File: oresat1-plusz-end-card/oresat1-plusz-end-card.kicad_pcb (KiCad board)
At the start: 4 copper layers, 99.8 x 94.6 mm, 103 parts, among them J1 J-SAMTEC-TFM-120-01-L-D-RA, J2 M55-7101242R, J3 M55-7101242R, J4 M55-7101242R, J5 M55-7101242R, J6 U.FL-R-SMT-1, Q1 DMP2240UDM, Q11 DMP2240UDM-7, Q2 PMV45EN, Q3 PMV45EN, Q4 PMV45EN, Q6 PMV45EN, Q9 DMP2240UDM-7, U11 MIC842LYC5, U12 MIC842LYC5, U2 MAX7310, U201 TS5A21366, U202 TS5A21366, U203 TS5A21366, U204 TS5A21366

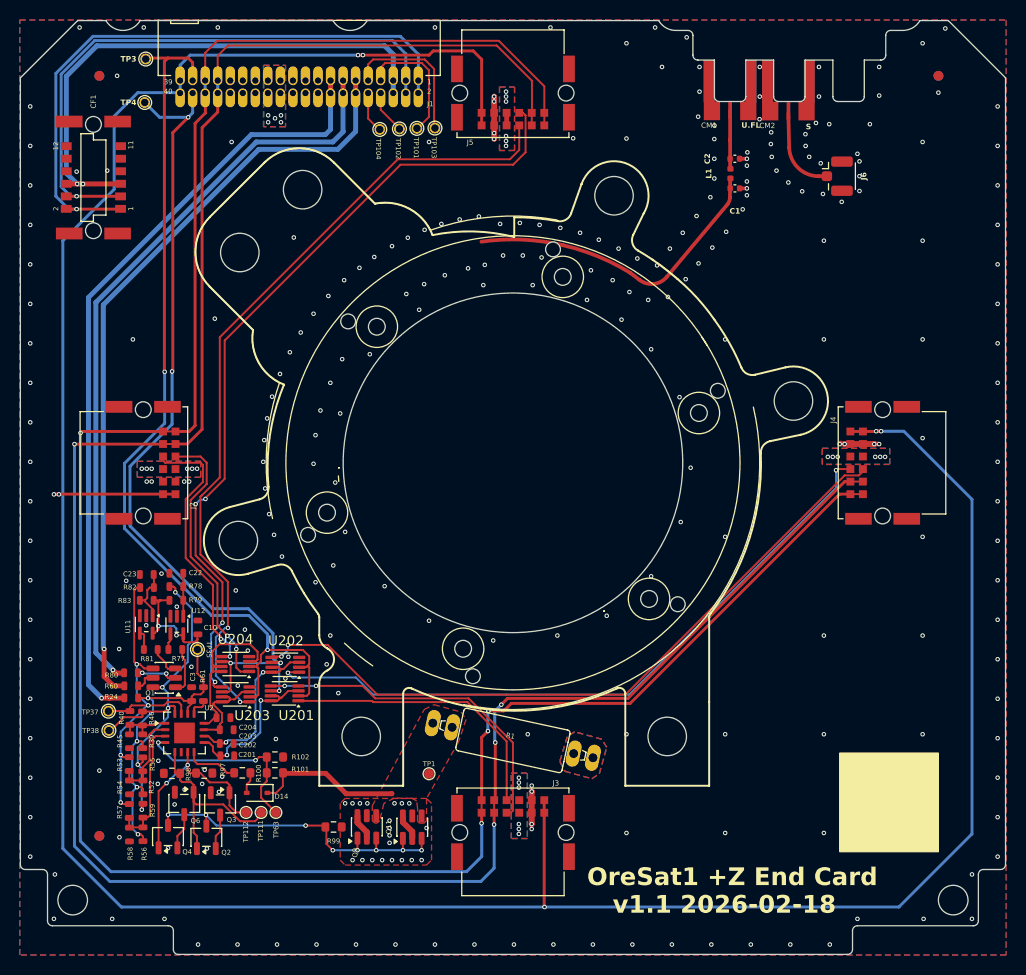
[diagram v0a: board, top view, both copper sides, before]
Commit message: Another round on the +Z End Card; ready for fab.
Brushed up RF paths and solder mask, cleaned up UART switches with closer bypass caps, cleaned up a lot of the zones, and lots of little polishing.
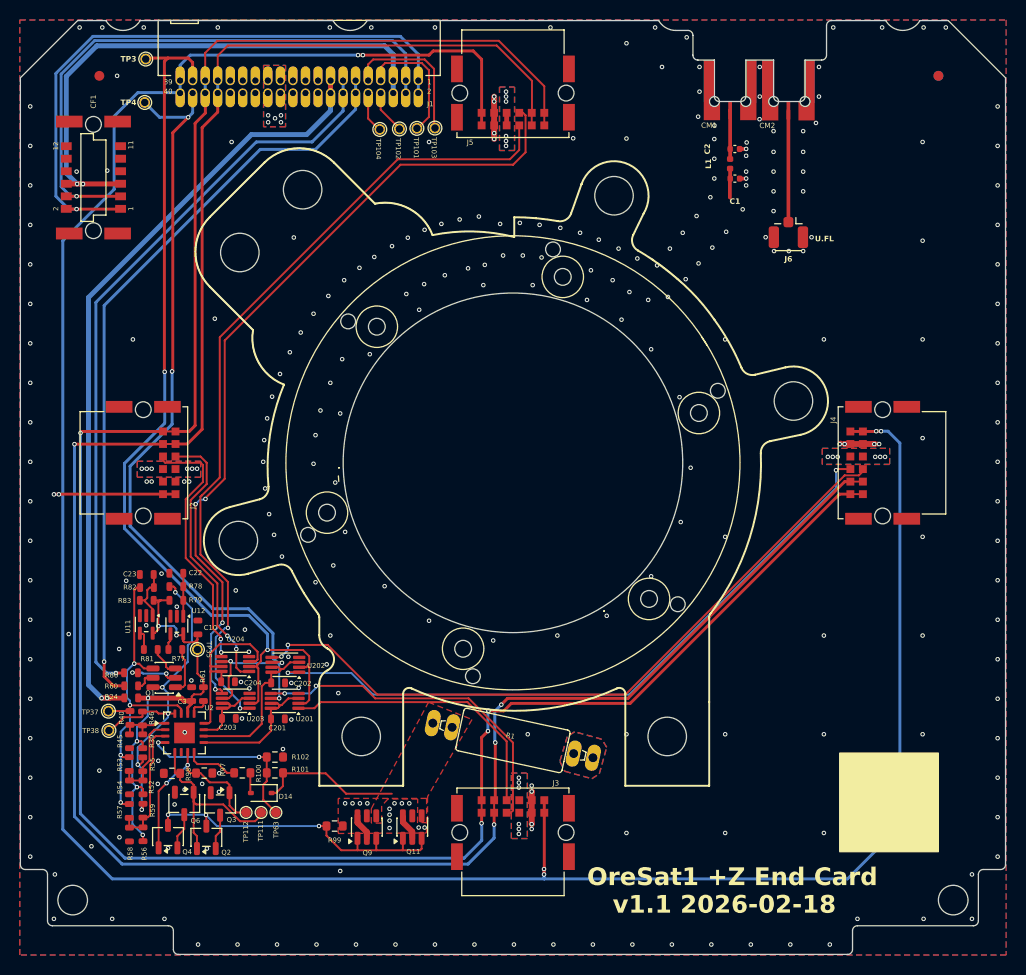
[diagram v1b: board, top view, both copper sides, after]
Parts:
- removed FID4, FID5, FID6: Fiducial, Fiducial:Fiducial_1mm_Mask2mm
- removed TP1: Test-Point, oresat-misc:TestPoint_Pad_D1.0mm
- PCB1: footprint oresat-pcbs:ORESAT-CARD-V1.3-3RF -> oresat-pcbs:ORESAT-CARD-V1.3-2RF-LEFT
- Q1: value DMP2240UDM -> DMP2240UDM-7
- Q2, Q3, Q4, Q6: value PMV45EN -> DMN3028LQ-7
- R39, R40, R45, R46, R52, R53, R54, R55, R56, R57, R58, R59: value 1k -> 100
- moved C202 8.05 mm to (124.7, 124.8)
- moved J6 7.55 mm to (176.4, 79.2), turned to -90 degrees
- moved C201 6.35 mm to (124.7, 128.4)
- moved C204 3.67 mm to (119.6, 124.7)
- moved C203 1.16 mm to (119.7, 128.4)
- moved L1 0.99 mm to (170.5, 72.2)
- moved C1 0.99 mm to (171.0, 73.7)
- moved C2 0.99 mm to (171.0, 70.7)
- moved U201 0.76 mm to (125.4, 126.6)
- moved U203 0.65 mm to (120.4, 126.6)
- moved D14 0.42 mm to (123.0, 135.9)
- moved R99 0.14 mm to (130.4, 139.3)
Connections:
- net /HELICAL renamed RF_HELICAL_ANT
- net /PATCH renamed /RF_PATCH
- net Net-(C2-Pad2) renamed /RF_HELICAL
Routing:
- net /~{SD}: track 296.9 -> 279.3 mm, vias 7 -> 8
- net /RF_PATCH: track 0.00 -> 11.3 mm
- net /CAN1_H: track 238.5 -> 233.5 mm
- net /CAN1_L: track 236.9 -> 233.2 mm
- net /C3_UART_RX: track 88.4 -> 90.8 mm
- net /OPD/PX_UART_EN: track 16.6 -> 14.6 mm, vias 2 -> 0
- net /OPD/MX_UART_EN: track 9.92 -> 8.00 mm
- net /OPD_SDA: track 78.1 -> 76.6 mm
- net /C3_UART_TX: track 94.3 -> 95.6 mm
- net /OPD/MY-UART-TX: track 27.6 -> 26.3 mm
- net Net-(Q1B-S): track 4.16 -> 5.29 mm
- net /OPD/OPD-SCL-INT: track 36.8 -> 35.6 mm
- net /RF_HELICAL: track 5.93 -> 4.93 mm
- net RF_HELICAL_ANT: track 32.2 -> 33.2 mm
- net /OPD/MY_UART_EN: track 17.3 -> 18.2 mm
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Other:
- outline, holes or cut-outs redrawn
- board text removed: "S"

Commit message: Align SMPM connectors better and add a bit more solder mask keepout
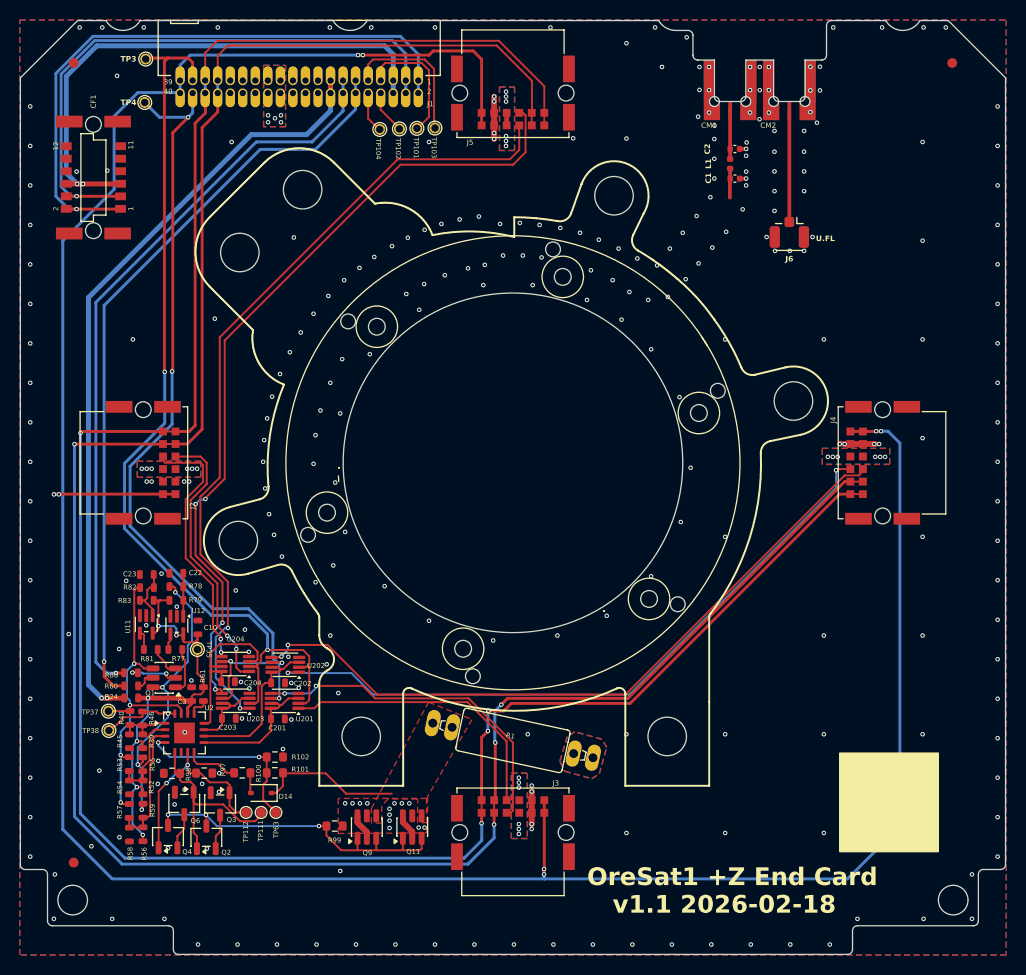
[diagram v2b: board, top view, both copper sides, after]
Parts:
- FID3: moved to F.Cu
- moved FID3 118.4 mm to (104.0, 143.0), turned to 0 degrees
- moved FID1 2.91 mm to (104.0, 62.0)
- moved FID2 1.91 mm to (193.0, 62.0)
- moved CM2 0.10 mm to (176.5, 61.7)
- moved J6 0.10 mm to (176.5, 79.2)
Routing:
- net GND: vias 273 -> 285

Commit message: v1.1 sent to fab
Updated 3D models of connectors, added missing capacitors, fixed footprints, polished schematic, upgraded to single README file with Makefile.
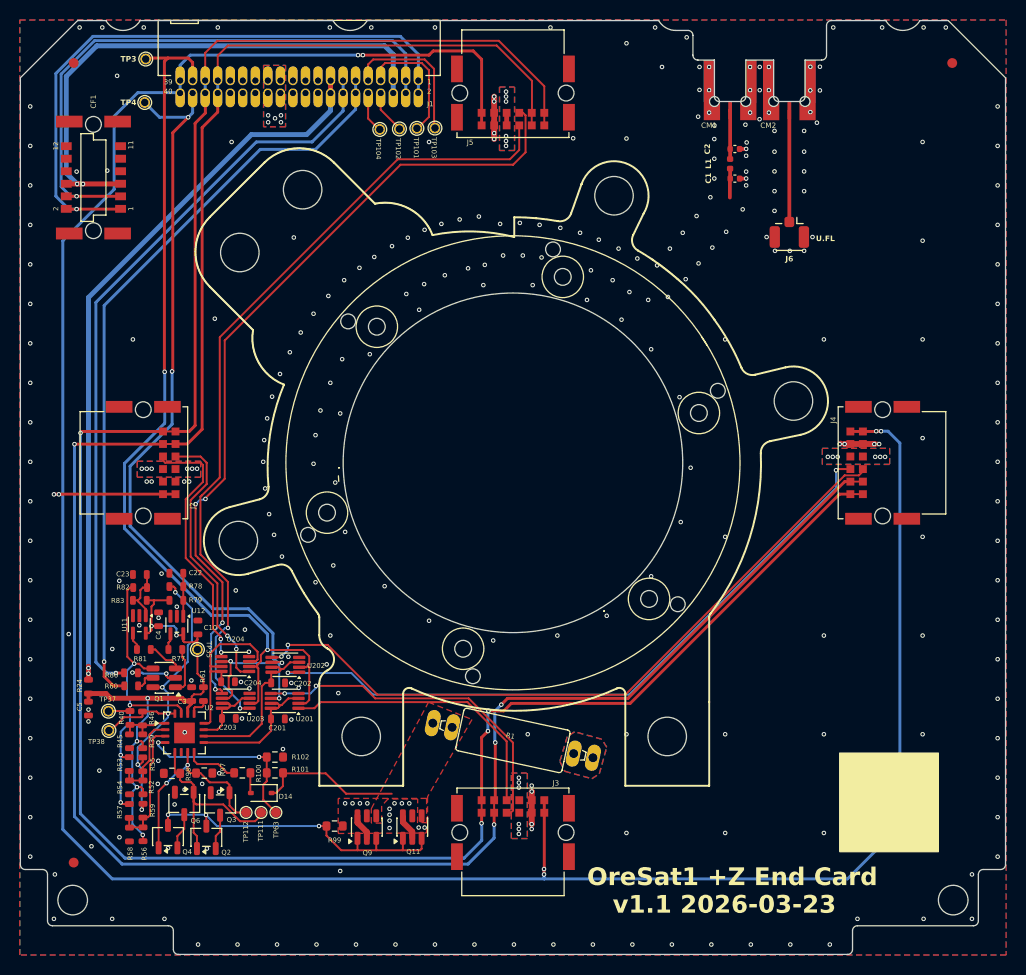
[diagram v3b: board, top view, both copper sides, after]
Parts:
- added C4: 100n, oresat-passives:0603-C-NOSILK, F.Cu at (112.6, 118.3)
- added C5: 1u, oresat-passives:0603-C-NOSILK, F.Cu at (105.5, 127.4)
- moved R24 4.48 mm to (105.5, 125.2), turned to -90 degrees
- moved R81 0.70 mm to (111.1, 121.4)
- moved R82 0.70 mm to (110.7, 115.1)
- moved U11 0.70 mm to (110.7, 118.9)
- moved C23 0.70 mm to (110.7, 113.8)
- moved R83 0.70 mm to (110.7, 116.4)
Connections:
- net /OPD/AD0 renamed /+Z EC OreSat Power Domain (OPD)/AD0
- net /OPD/AD1 renamed /+Z EC OreSat Power Domain (OPD)/AD1
- net /OPD/AD2 renamed /+Z EC OreSat Power Domain (OPD)/AD2
- net /OPD/FIRE_HELICAL_1 renamed /+Z EC OreSat Power Domain (OPD)/FIRE_HELICAL_1
- net /OPD/FIRE_HELICAL_2 renamed /+Z EC OreSat Power Domain (OPD)/FIRE_HELICAL_2
- net /OPD/HELICAL_DEPLOY renamed /+Z EC OreSat Power Domain (OPD)/HELICAL_DEPLOY
- net /OPD/MX-UART-RX renamed /+Z EC OreSat Power Domain (OPD)/MX-UART-RX
- net /OPD/MX-UART-TX renamed /+Z EC OreSat Power Domain (OPD)/MX-UART-TX
- net /OPD/MX_UART_EN renamed /+Z EC OreSat Power Domain (OPD)/MX_UART_EN
- net /OPD/MY-UART-RX renamed /+Z EC OreSat Power Domain (OPD)/MY-UART-RX
- net /OPD/MY-UART-TX renamed /+Z EC OreSat Power Domain (OPD)/MY-UART-TX
- net /OPD/MY_UART_EN renamed /+Z EC OreSat Power Domain (OPD)/MY_UART_EN
- net /OPD/OPD-SCL-INT renamed /+Z EC OreSat Power Domain (OPD)/OPD-SCL-INT
- net /OPD/OPD-SDA-INT renamed /+Z EC OreSat Power Domain (OPD)/OPD-SDA-INT
- net /OPD/PX-UART-RX renamed /+Z EC OreSat Power Domain (OPD)/PX-UART-RX
- net /OPD/PX-UART-TX renamed /+Z EC OreSat Power Domain (OPD)/PX-UART-TX
- net /OPD/PX_UART_EN renamed /+Z EC OreSat Power Domain (OPD)/PX_UART_EN
- net /OPD/PY-UART-RX renamed /+Z EC OreSat Power Domain (OPD)/PY-UART-RX
- net /OPD/PY-UART-TX renamed /+Z EC OreSat Power Domain (OPD)/PY-UART-TX
- net /OPD/PY_UART_EN renamed /+Z EC OreSat Power Domain (OPD)/PY_UART_EN
- net /OPD/READ_HELICAL renamed /+Z EC OreSat Power Domain (OPD)/READ_HELICAL
- net /OPD/TEST_HELICAL renamed /+Z EC OreSat Power Domain (OPD)/TEST_HELICAL
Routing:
- net VPD: track 44.5 -> 52.7 mm
- net /OPD_PWR: track 79.4 -> 75.5 mm
- net GND: vias 285 -> 289
